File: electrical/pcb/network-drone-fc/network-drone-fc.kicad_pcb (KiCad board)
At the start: 4 copper layers, 36 x 39 mm, 83 parts, among them J1 U.FL-R-SMT-1, J2 TYPE-C 16PIN 2MD, J3 U.FL GPS, J4 ESC, J5 I2C port, J7 Charging board, U1 ESP32-S3FN8, U2 USBLC6-2SC6, U3 AP63205WU-7, U4 TLV75733PDRVR, U5 TPS7A2033PDBVR, U6 ICM-42688-P, U7 BMP581, U8 MAX-M10S, X1 Q22FA12800101

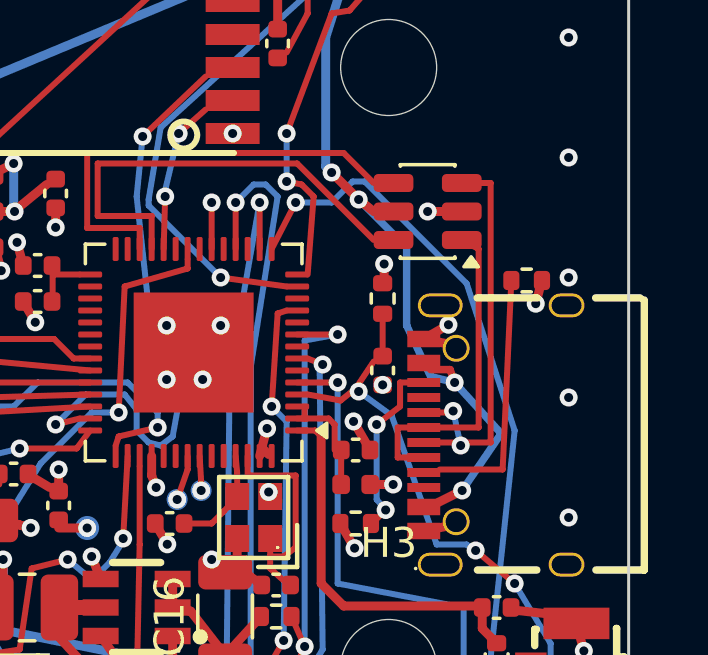
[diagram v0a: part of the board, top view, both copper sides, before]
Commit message: PCB: hand reroutes (ESC telemetry and nearby tracks)
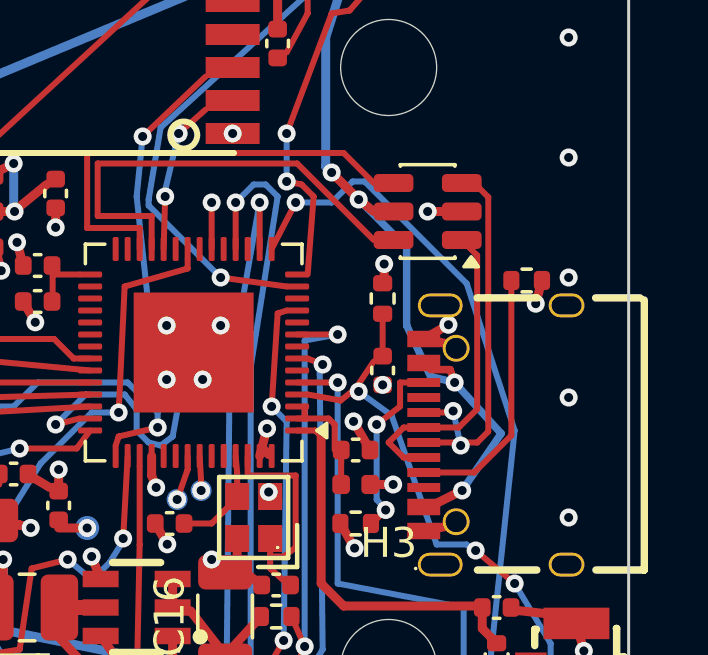
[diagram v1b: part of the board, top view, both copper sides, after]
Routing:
- net D+: track 14.1 -> 13.5 mm
- net D-: track 11.2 -> 10.6 mm
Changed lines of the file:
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@@
 	)
 	(segment
-		(start 111.7 103.4)
-		(end 113.8 103.4)
+		(start 114.09 102.263963)
+		(end 114.09 97.1)
 		(width 0.2)
 		(layer "F.Cu")
@@
 	)
 	(segment
-		(start 113.8 103.4)
-		(end 114.09 97.1)
+		(start 112.853963 103.5)
+		(end 114.09 102.263963)
+		(width 0.2)
+		(layer "F.Cu")
+		(net 1)
+	)
+	(segment
+		(start 111.17 103.5)
+		(end 112.853963 103.5)
 		(width 0.2)
 		(layer "F.Cu")
@@
 	)
 	(segment
-		(start 113.4 93.85)
-		(end 112.4375 93.85)
-		(width 0.2)
-		(layer "F.Cu")
-		(net 6)
-	)
-	(segment
 		(start 111.17 101.5)
 		(end 112.1 101.5)
@@
 	)
 	(segment
-		(start 113.4 102.5)
-		(end 113.4 93.85)
+		(start 113.321 102.132963)
+		(end 112.953963 102.5)
 		(width 0.2)
 		(layer "F.Cu")
@@
 	)
 	(segment
-		(start 111.17 102.5)
-		(end 113.4 102.5)
+		(start 113.321 94.321)
+		(end 113.321 102.132963)
+		(width 0.2)
+		(layer "F.Cu")
+		(net 6)
+	)
+	(segment
+		(start 112.4375 93.85)
+		(end 112.4375 93.9375)
+		(width 0.2)
+		(layer "F.Cu")
+		(net 6)
+	)
+	(segment
+		(start 113 94)
+		(end 113.321 94.321)
+		(width 0.2)
+		(layer "F.Cu")
+		(net 6)
+	)
+	(segment
+		(start 112.953963 102.5)
+		(end 111.17 102.5)
+		(width 0.2)
+		(layer "F.Cu")
+		(net 6)
+	)
+	(segment
+		(start 112.4375 93.9375)
+		(end 112.5 94)
+		(width 0.2)
+		(layer "F.Cu")
+		(net 6)
+	)
+	(segment
+		(start 112.5 94)
+		(end 113 94)
 		(width 0.2)
 		(layer "F.Cu")
@@
 	)
 	(segment
-		(start 110.3 102)
+		(start 112.951 96.2635)
+		(end 112.951 101.385806)
+		(width 0.2)
+		(layer "F.Cu")
+		(net 7)
+	)
+	(segment
+		(start 110.5 102)
+		(end 110 102.5)
+		(width 0.2)
+		(layer "F.Cu")
+		(net 7)
+	)
+	(segment
+		(start 111.17 102)
+		(end 110.5 102)
+		(width 0.2)
+		(layer "F.Cu")
+		(net 7)
+	)
+	(segment
+		(start 110 102.5)
+		(end 110.5 103)
+		(width 0.2)
+		(layer "F.Cu")
+		(net 7)
+	)
+	(segment
+		(start 112.4375 95.75)
+		(end 112.951 96.2635)
+		(width 0.2)
+		(layer "F.Cu")
+		(net 7)
+	)
+	(segment
+		(start 112.951 101.385806)
+		(end 112.336806 102)
+		(width 0.2)
+		(layer "F.Cu")
+		(net 7)
+	)
+	(segment
+		(start 110.5 103)
+		(end 111.17 103)
+		(width 0.2)
+		(layer "F.Cu")
+		(net 7)
+	)
+	(segment
+		(start 112.336806 102)
 		(end 111.17 102)
 		(width 0.2)
 		(layer "F.Cu")
-		(net 7)
-	)
-	(segment
-		(start 110.3 103)
-		(end 110.3 102)
-		(width 0.2)
-		(layer "F.Cu")
-		(net 7)
-	)
-	(segment
-		(start 111.17 103)
-		(end 110.3 103)
-		(width 0.2)
-		(layer "F.Cu")
-		(net 7)
-	)
-	(segment
-		(start 111.17 102)
-		(end 113 102)
-		(width 0.2)
-		(layer "F.Cu")
-		(net 7)
-	)
-	(segment
-		(start 113 96.05)
-		(end 112.4375 95.75)
-		(width 0.2)
-		(layer "F.Cu")
-		(net 7)
-	)
-	(segment
-		(start 113 102)
-		(end 113 96.05)
-		(width 0.2)
-		(layer "F.Cu")

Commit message: PCB: J6 radio port in the bottom-right corner, J5 power pin on +5V, own 5 V branch from the buck output
159 vias. DRC 0 errors; one new courtyard warning where J6's outline is 0.2 mm inside the H3 keep-out (pads and body clear it). Schematic and board match on all 296 pins.
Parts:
- added J6: Radio UART 5V, tar_fc:JST_SH_BM04B-SRSS-TB_1x04_Vertical, F.Cu at (113.9, 115.4)
- J5: value I2C port -> Sensor port 5V I2C
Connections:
- J5 pad 1: +3V3 -> +5V
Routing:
- net +5V: track 47.7 -> 86.7 mm, vias 6 -> 10
- net ESC_CUR: track 24.2 -> 33.4 mm, vias 3 -> 4
- net GND: track 55.3 -> 61.1 mm, vias 82 -> 81
- net ESC_TELEM: track 40.4 -> 45.1 mm
- net +3V3: vias 14 -> 13
